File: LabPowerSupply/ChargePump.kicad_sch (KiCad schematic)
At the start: 7 parts

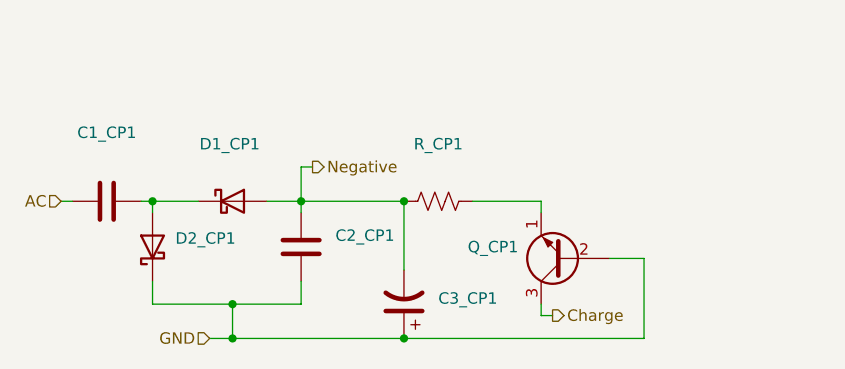
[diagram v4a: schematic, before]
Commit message: Added mcu capacitors, split 5v inductors
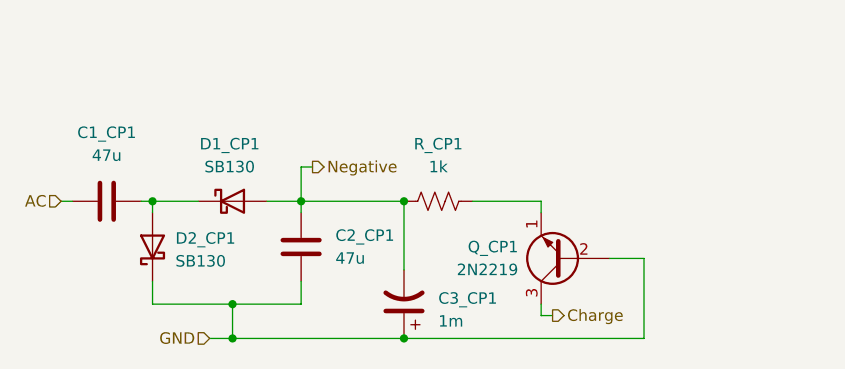
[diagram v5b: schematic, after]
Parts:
- C1_CP1, C2_CP1: value (none) -> 47u; footprint (none) -> Capacitor_THT:C_Disc_D6.0mm_W2.5mm_P5.00mm
- C3_CP1: value (none) -> 1m; footprint (none) -> Capacitor_THT:CP_Radial_D10.0mm_P5.00mm
- D1_CP1, D2_CP1: value (none) -> SB130; footprint (none) -> Diode_THT:D_DO-41_SOD81_P10.16mm_Horizontal
- Q_CP1: value (none) -> 2N2219; footprint (none) -> Package_TO_SOT_THT:TO-92_Inline
- R_CP1: value (none) -> 1k; footprint (none) -> Resistor_SMD:R_0603_1608Metric
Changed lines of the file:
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@@
       (effects (font (size 1.27 1.27)) (justify left))
     )
-    (property "Value" "" (id 1) (at 148.59 106.6799 0)
+    (property "Value" "47u" (id 1) (at 148.59 106.6799 0)
       (effects (font (size 1.27 1.27)) (justify left))
     )
-    (property "Footprint" "" (id 2) (at 145.7452 109.22 0)
+    (property "Footprint" "Capacitor_THT:C_Disc_D6.0mm_W2.5mm_P5.00mm" (id 2) (at 145.7452 109.22 0)
       (effects (font (size 1.27 1.27)) hide)
     )
@@
     (in_bom yes) (on_board yes) (fields_autoplaced)
     (property "Reference" "C1_CP1" (id 0) (at 123.19 92.71 90))
-    (property "Value" "" (id 1) (at 123.19 95.25 90))
-    (property "Footprint" "" (id 2) (at 127 99.3648 0)
+    (property "Value" "47u" (id 1) (at 123.19 95.25 90))
+    (property "Footprint" "Capacitor_THT:C_Disc_D6.0mm_W2.5mm_P5.00mm" (id 2) (at 127 99.3648 0)
       (effects (font (size 1.27 1.27)) hide)
     )
@@
       (effects (font (size 1.27 1.27)) (justify right))
     )
-    (property "Value" "" (id 1) (at 130.81 106.9974 90)
+    (property "Value" "SB130" (id 1) (at 130.81 106.9974 90)
       (effects (font (size 1.27 1.27)) (justify right))
     )
-    (property "Footprint" "" (id 2) (at 132.715 105.41 0)
+    (property "Footprint" "Diode_THT:D_DO-41_SOD81_P10.16mm_Horizontal" (id 2) (at 132.715 105.41 0)
       (effects (font (size 1.27 1.27)) hide)
     )
@@
       (effects (font (size 1.27 1.27)) (justify left))
     )
-    (property "Value" "" (id 1) (at 168.91 107.9499 0)
+    (property "Value" "2N2219" (id 1) (at 168.91 107.9499 0)
       (effects (font (size 1.27 1.27)) (justify left))
     )
-    (property "Footprint" "" (id 2) (at 168.91 104.775 0)
+    (property "Footprint" "Package_TO_SOT_THT:TO-92_Inline" (id 2) (at 168.91 104.775 0)
       (effects (font (size 1.27 1.27) italic) (justify left) hide)
     )
@@
     (in_bom yes) (on_board yes) (fields_autoplaced)
     (property "Reference" "D1_CP1" (id 0) (at 136.8425 93.98 0))
-    (property "Value" "" (id 1) (at 136.8425 96.52 0))
-    (property "Footprint" "" (id 2) (at 137.16 104.775 0)
+    (property "Value" "SB130" (id 1) (at 136.8425 96.52 0))
+    (property "Footprint" "Diode_THT:D_DO-41_SOD81_P10.16mm_Horizontal" (id 2) (at 137.16 104.775 0)
       (effects (font (size 1.27 1.27)) hide)
     )
@@
       (effects (font (size 1.27 1.27)) (justify right))
     )
-    (property "Value" "" (id 1) (at 160.02 113.6649 0)
+    (property "Value" "1m" (id 1) (at 160.02 113.6649 0)
       (effects (font (size 1.27 1.27)) (justify right))
     )
-    (property "Footprint" "" (id 2) (at 156.21 111.76 0)
+    (property "Footprint" "Capacitor_THT:CP_Radial_D10.0mm_P5.00mm" (id 2) (at 156.21 111.76 0)
       (effects (font (size 1.27 1.27)) hide)
     )
@@
     (in_bom yes) (on_board yes) (fields_autoplaced)
     (property "Reference" "R_CP1" (id 0) (at 160.02 93.98 90))
-    (property "Value" "" (id 1) (at 160.02 96.52 90))
-    (property "Footprint" "" (id 2) (at 160.274 99.314 90)
+    (property "Value" "1k" (id 1) (at 160.02 96.52 90))
+    (property "Footprint" "Resistor_SMD:R_0603_1608Metric" (id 2) (at 160.274 99.314 90)
       (effects (font (size 1.27 1.27)) hide)
     )

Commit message: Changed most parts to smd
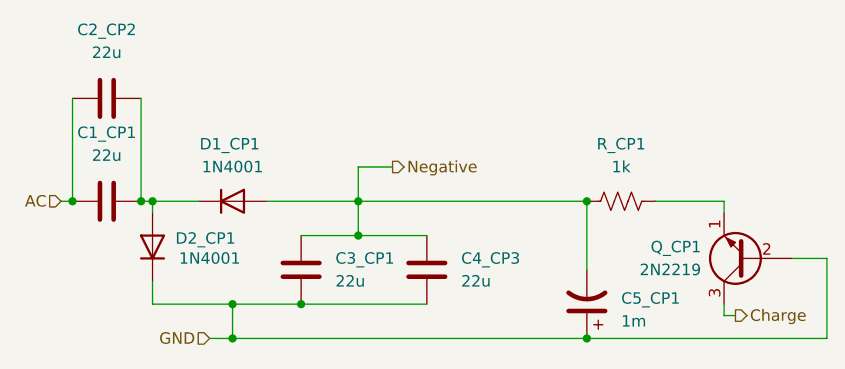
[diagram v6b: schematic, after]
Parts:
- added C2_CP2, C4_CP3: 22u, Capacitor_SMD:C_0805_2012Metric, symbol Device:C
- C1_CP1: value 47u -> 22u; footprint Capacitor_THT:C_Disc_D6.0mm_W2.5mm_P5.00mm -> Capacitor_SMD:C_0805_2012Metric
- C3_CP1: renamed from C2_CP1; value 47u -> 22u; footprint Capacitor_THT:C_Disc_D6.0mm_W2.5mm_P5.00mm -> Capacitor_SMD:C_0805_2012Metric
- D1_CP1, D2_CP1: value SB130 -> 1N4001; footprint Diode_THT:D_DO-41_SOD81_P10.16mm_Horizontal -> Diode_SMD:D_SMA; symbol Diode:SB130 -> Diode:1N4001
- renumbered C3_CP1 to C5_CP1
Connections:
- net AC: now also C2_CP2.1
- net GND: now also C4_CP3.2
- net Negative: now also C4_CP3.1
- net at C1_CP1.2, D1_CP1.1 (K), D2_CP1.2 (A): now also C2_CP2.2
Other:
- moved on the sheet: C3_CP1, C5_CP1, Q_CP1, R_CP1

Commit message: Fixed oscillator caps, began changing resistors to more common values
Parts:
- renumbered C2_CP2 to C2_CP1, C4_CP3 to C4_CP1
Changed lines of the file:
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@@
   (symbol (lib_id "Device:C") (at 158.75 107.95 0) (unit 1)
     (in_bom yes) (on_board yes) (fields_autoplaced)
-    (property "Reference" "C4_CP3" (id 0) (at 162.56 106.6799 0)
+    (property "Reference" "C4_CP1" (id 0) (at 162.56 106.6799 0)
       (effects (font (size 1.27 1.27)) (justify left))
     )
@@
   (symbol (lib_id "Device:C") (at 123.19 88.9 90) (unit 1)
     (in_bom yes) (on_board yes) (fields_autoplaced)
-    (property "Reference" "C2_CP2" (id 0) (at 123.19 81.28 90))
+    (property "Reference" "C2_CP1" (id 0) (at 123.19 81.28 90))
     (property "Value" "22u" (id 1) (at 123.19 83.82 90))
     (property "Footprint" "Capacitor_SMD:C_0805_2012Metric" (id 2) (at 127 87.9348 0)

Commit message: Made BJT SMD
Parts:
- Q_CP1: footprint Package_TO_SOT_THT:TO-92_Inline -> (none)
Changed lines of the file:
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@@
       (effects (font (size 1.27 1.27)) (justify left))
     )
-    (property "Footprint" "Package_TO_SOT_THT:TO-92_Inline" (id 2) (at 189.23 104.775 0)
+    (property "Footprint" "" (id 2) (at 189.23 104.775 0)
       (effects (font (size 1.27 1.27) italic) (justify left) hide)
     )
